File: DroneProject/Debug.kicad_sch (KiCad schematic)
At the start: 6 parts

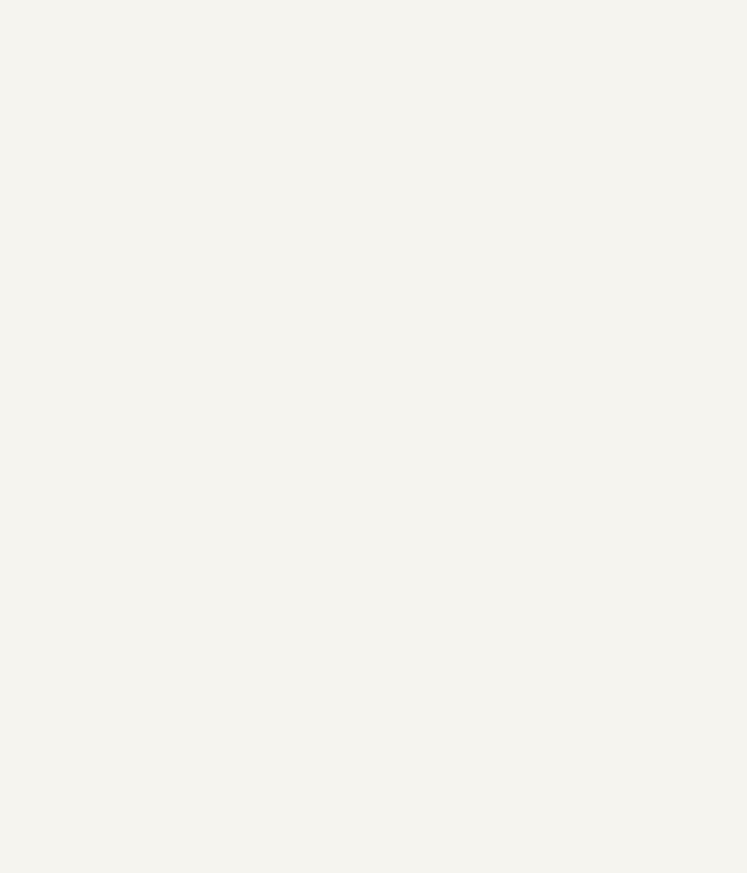
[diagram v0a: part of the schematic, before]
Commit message: Added test points
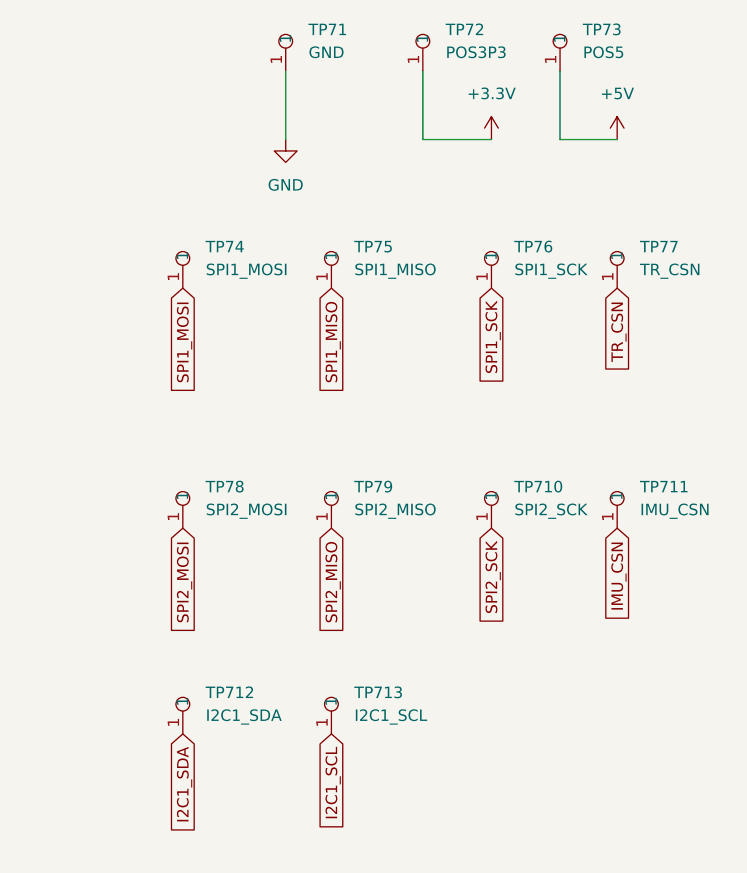
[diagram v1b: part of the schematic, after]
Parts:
- added TP71: GND, Library:Testpoint 1.6mm x 0.8mm, symbol Global:Testpoint
- added TP710: SPI2_SCK, Library:Testpoint 1.6mm x 0.8mm, symbol Global:Testpoint
- added TP711: IMU_CSN, Library:Testpoint 1.6mm x 0.8mm, symbol Global:Testpoint
- added TP712: I2C1_SDA, Library:Testpoint 1.6mm x 0.8mm, symbol Global:Testpoint
- added TP713: I2C1_SCL, Library:Testpoint 1.6mm x 0.8mm, symbol Global:Testpoint
- added TP72: POS3P3, Library:Testpoint 1.6mm x 0.8mm, symbol Global:Testpoint
- added TP73: POS5, Library:Testpoint 1.6mm x 0.8mm, symbol Global:Testpoint
- added TP74: SPI1_MOSI, Library:Testpoint 1.6mm x 0.8mm, symbol Global:Testpoint
- added TP75: SPI1_MISO, Library:Testpoint 1.6mm x 0.8mm, symbol Global:Testpoint
- added TP76: SPI1_SCK, Library:Testpoint 1.6mm x 0.8mm, symbol Global:Testpoint
- added TP77: TR_CSN, Library:Testpoint 1.6mm x 0.8mm, symbol Global:Testpoint
- added TP78: SPI2_MOSI, Library:Testpoint 1.6mm x 0.8mm, symbol Global:Testpoint
- added TP79: SPI2_MISO, Library:Testpoint 1.6mm x 0.8mm, symbol Global:Testpoint
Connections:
- net +3.3V: now also TP72.1
- net GND: now also TP71.1
- new net +5V: TP73.1
- new net I2C1_SCL: TP713.1
- new net I2C1_SDA: TP712.1
- new net IMU_CSN: TP711.1
- new net SPI1_MISO: TP75.1
- new net SPI1_MOSI: TP74.1
- new net SPI1_SCK: TP76.1
- new net SPI2_MISO: TP79.1
- new net SPI2_MOSI: TP78.1
- new net SPI2_SCK: TP710.1
- new net TR_CSN: TP77.1

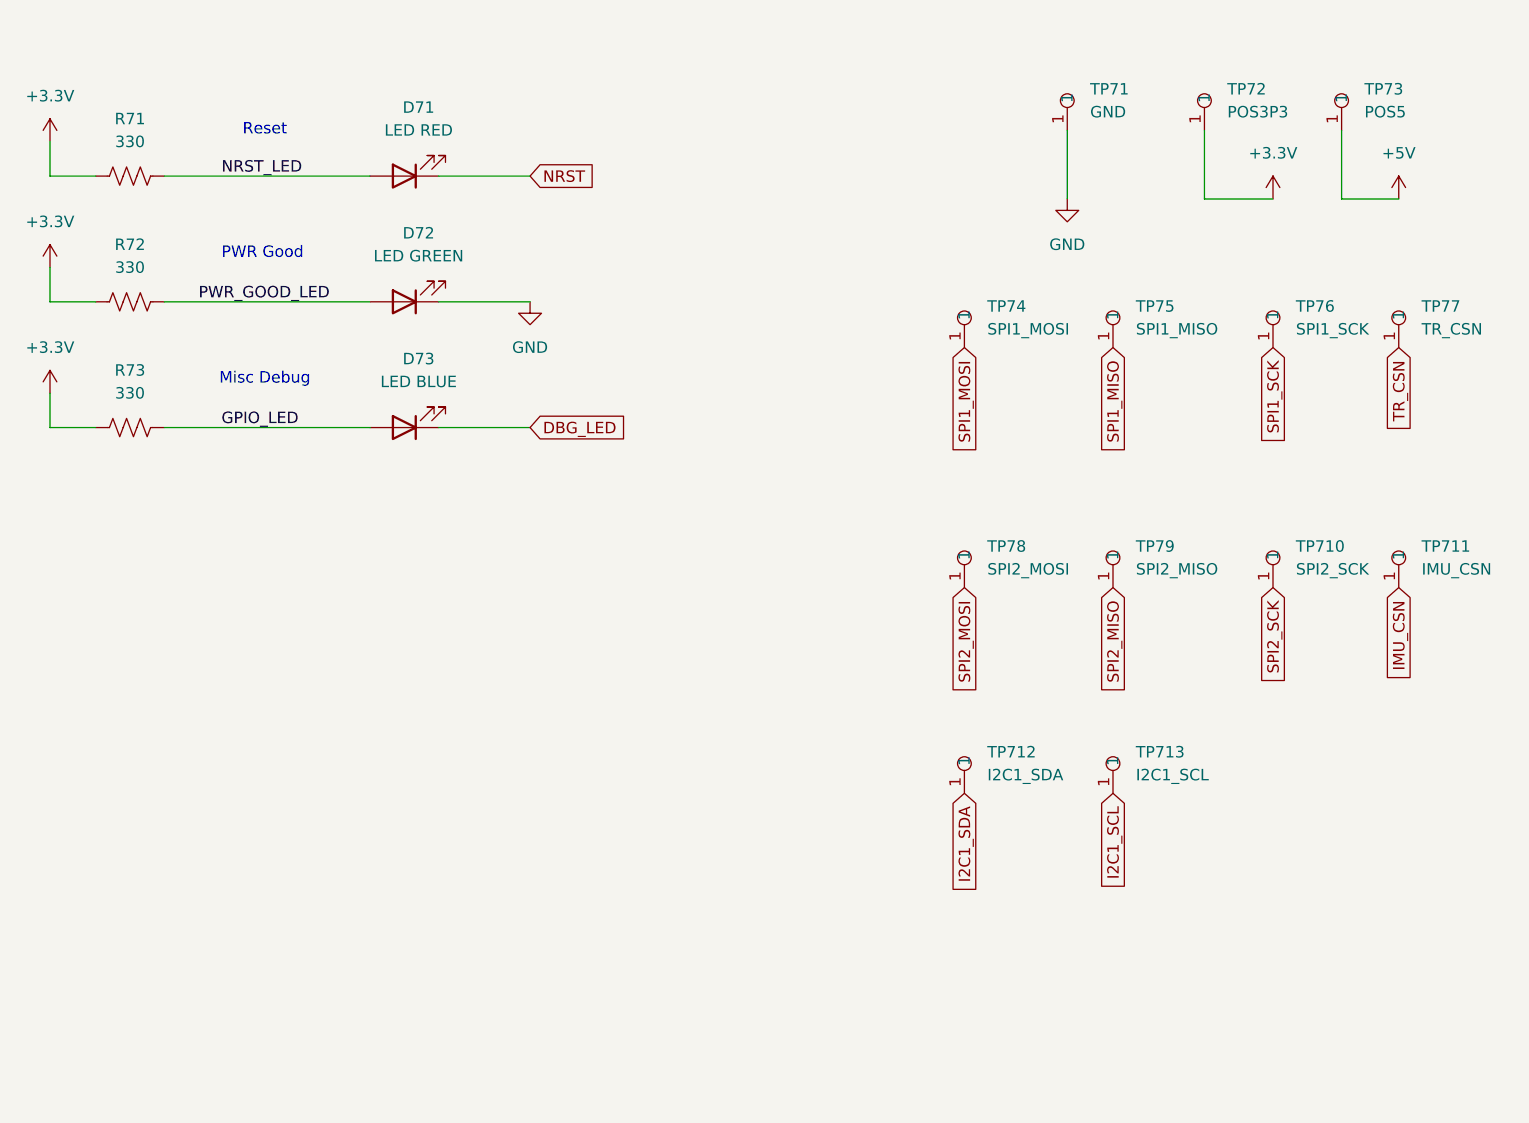
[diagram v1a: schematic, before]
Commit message: Added mounting holes and some more testpoints.  Also started on PCB with dimesions and mounting holes measured and placed
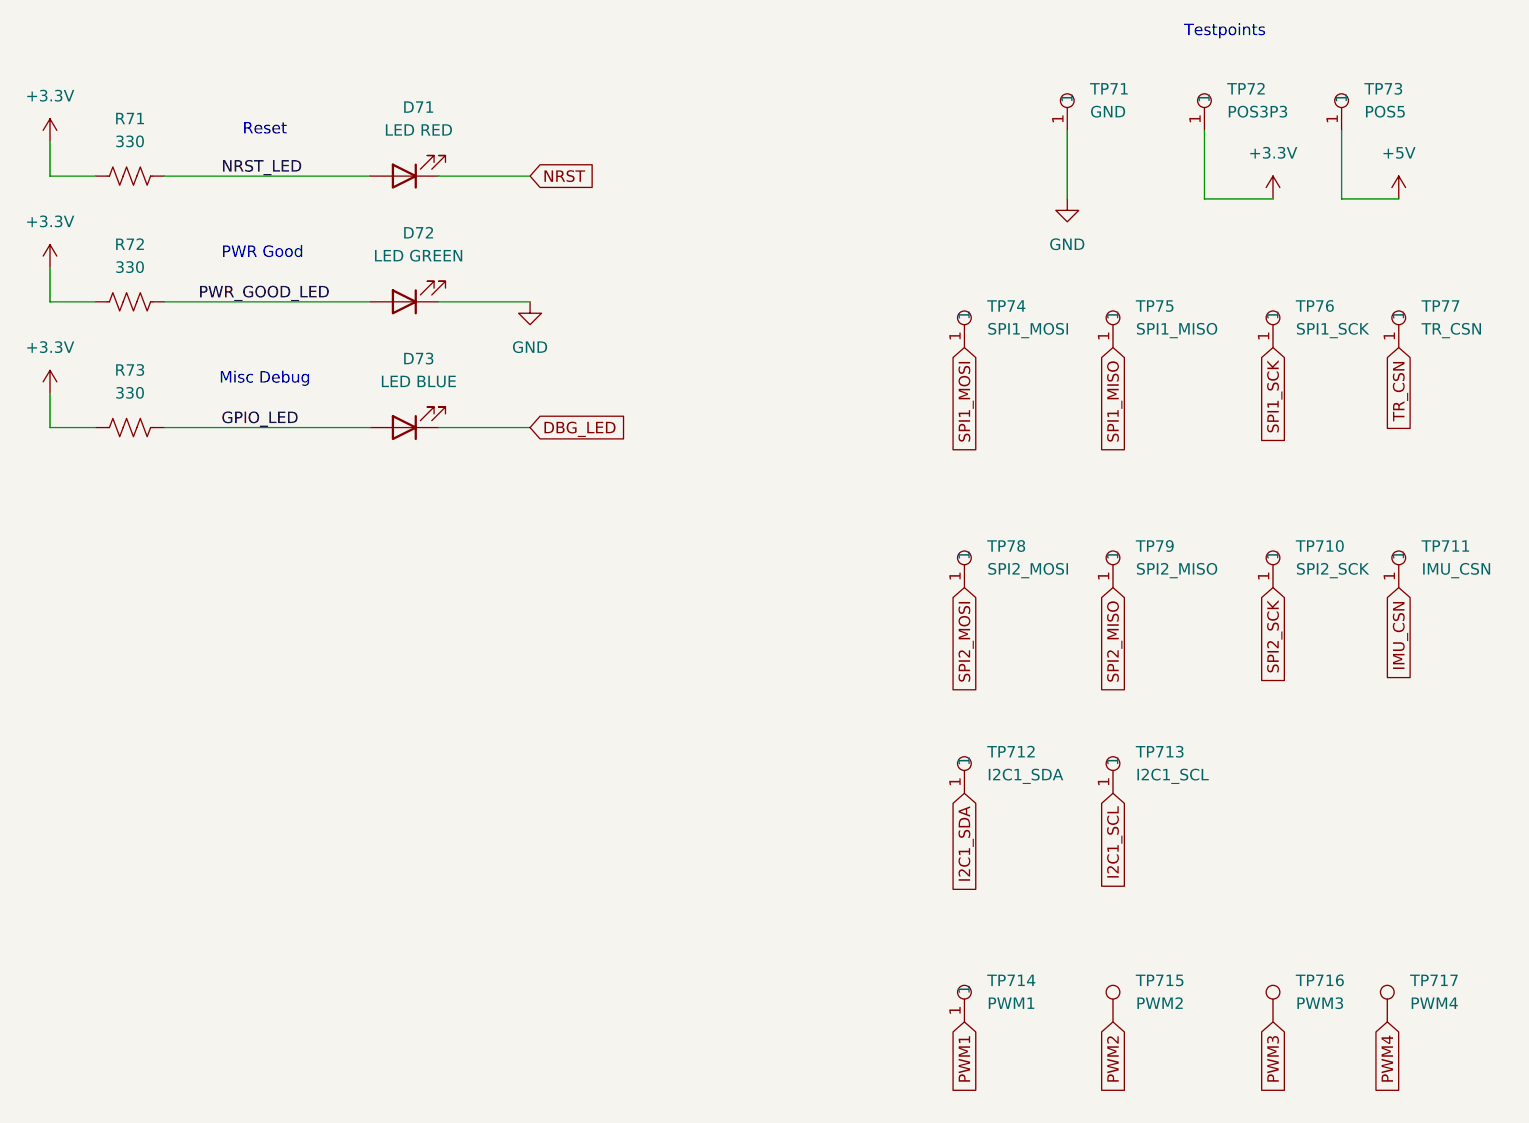
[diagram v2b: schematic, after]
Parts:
- added TP714: PWM1, Library:Testpoint 1.6mm x 0.8mm, symbol Global:Testpoint
- added TP715: PWM2, symbol Connector:TestPoint
- added TP716: PWM3, symbol Connector:TestPoint
- added TP717: PWM4, symbol Connector:TestPoint
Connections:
- new net PWM1: TP714.1
- new net PWM2: TP715.1
- new net PWM3: TP716.1
- new net PWM4: TP717.1
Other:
- note added: "Testpoints"

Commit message: Finished initial PCB layout.  However decided to go ahead and add the motor drivers for the first prototype anyways.  Re-did the reverse-polarity detection to use an NMOS instead of a PMOS.  Added sheets for each motor, still need to decide on parts.
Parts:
- TP715, TP716, TP717: footprint (none) -> Library:Testpoint 1.6mm x 0.8mm
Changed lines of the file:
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@@
 			)
 		)
-		(property "Footprint" ""
+		(property "Footprint" "Library:Testpoint 1.6mm x 0.8mm"
 			(at 152.4 132.08 0)
 			(effects
@@
 			)
 		)
-		(property "Footprint" ""
+		(property "Footprint" "Library:Testpoint 1.6mm x 0.8mm"
 			(at 182.88 132.08 0)
 			(effects
@@
 			)
 		)
-		(property "Footprint" ""
+		(property "Footprint" "Library:Testpoint 1.6mm x 0.8mm"
 			(at 170.18 132.08 0)
 			(effects

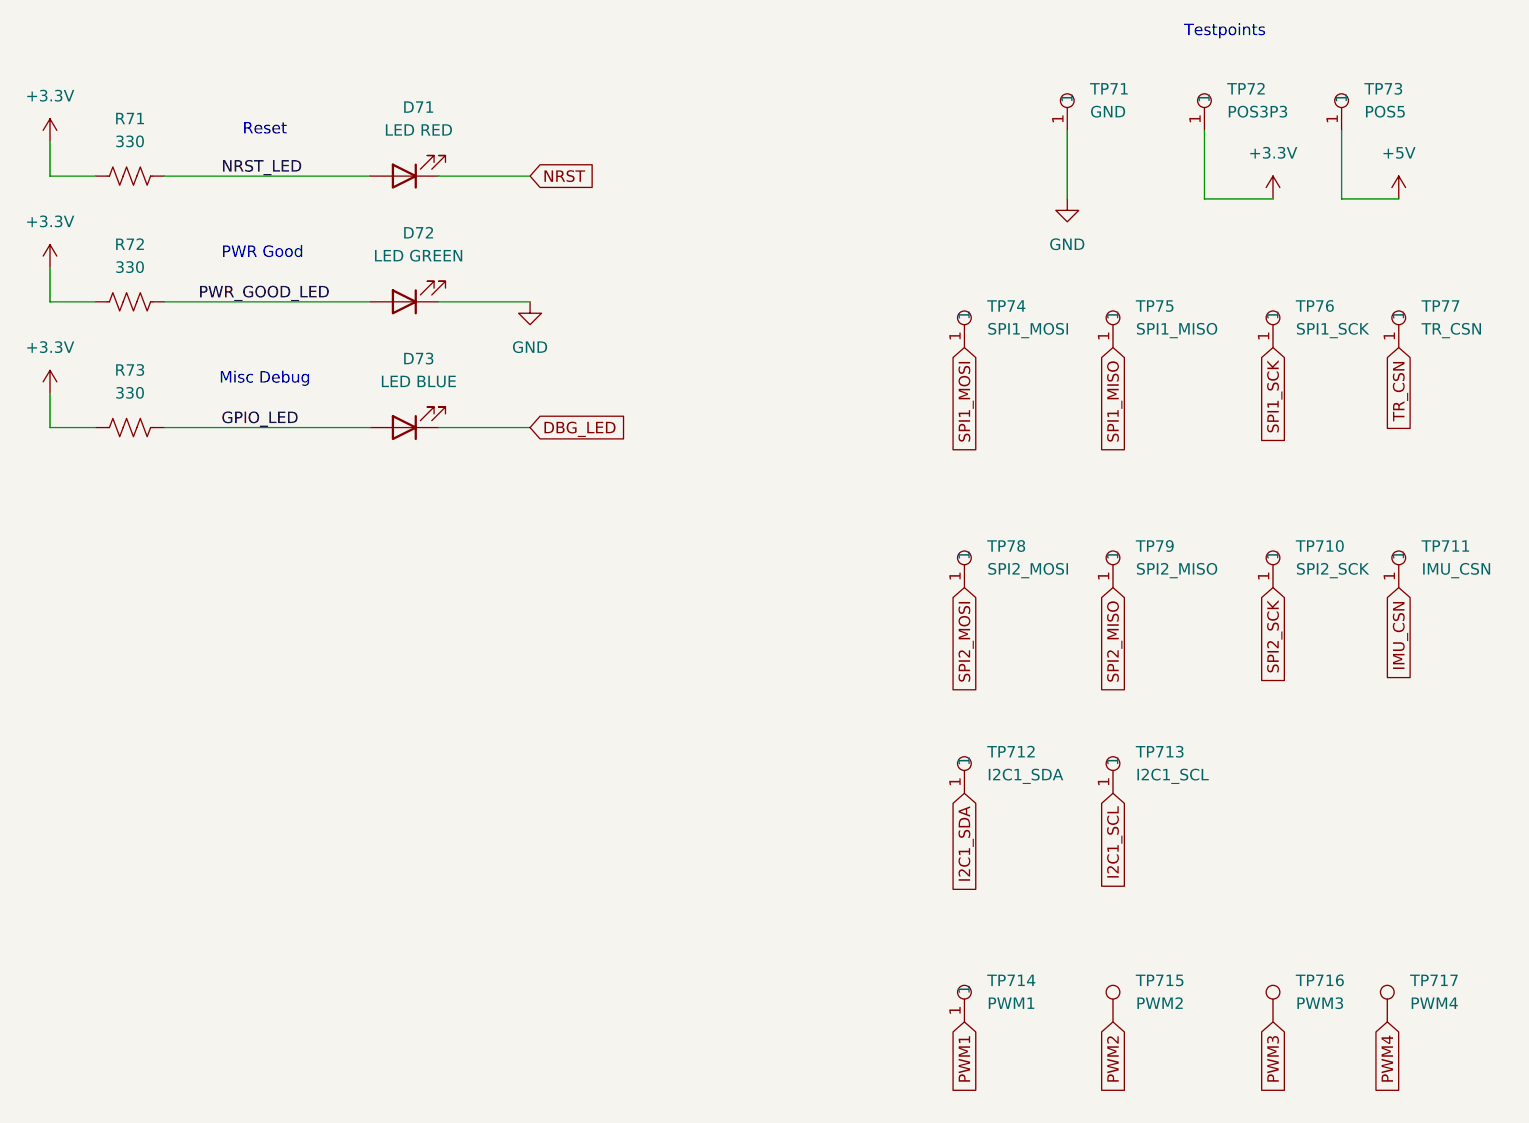
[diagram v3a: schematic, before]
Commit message: Added a second MCU for motor control.  Removed 5V rail.  Added COM switching for SWD and UART external headers
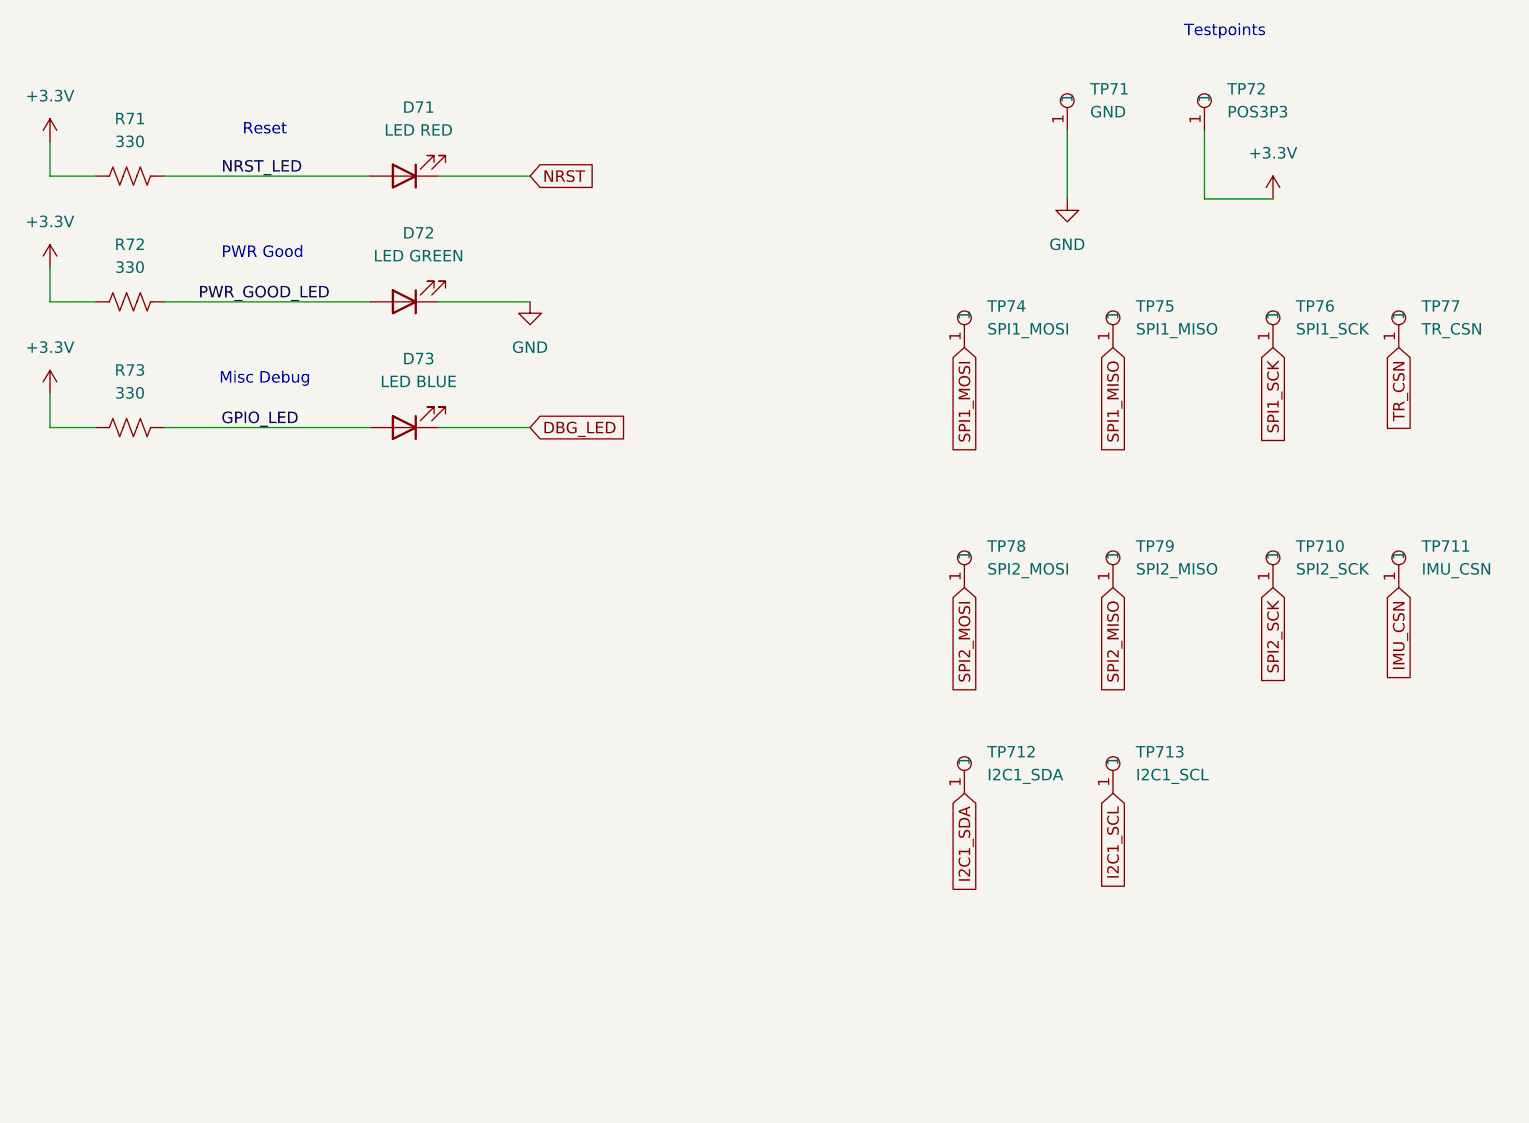
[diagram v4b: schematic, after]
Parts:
- removed TP714: PWM1, Library:Testpoint 1.6mm x 0.8mm, symbol Global:Testpoint
- removed TP715: PWM2, Library:Testpoint 1.6mm x 0.8mm, symbol Connector:TestPoint
- removed TP716: PWM3, Library:Testpoint 1.6mm x 0.8mm, symbol Connector:TestPoint
- removed TP717: PWM4, Library:Testpoint 1.6mm x 0.8mm, symbol Connector:TestPoint
- removed TP73: POS5, Library:Testpoint 1.6mm x 0.8mm, symbol Global:Testpoint
